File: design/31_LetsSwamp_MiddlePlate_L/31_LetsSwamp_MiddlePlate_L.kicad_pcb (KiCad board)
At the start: 2 copper layers, 122.6 x 85.3 mm, 0 parts

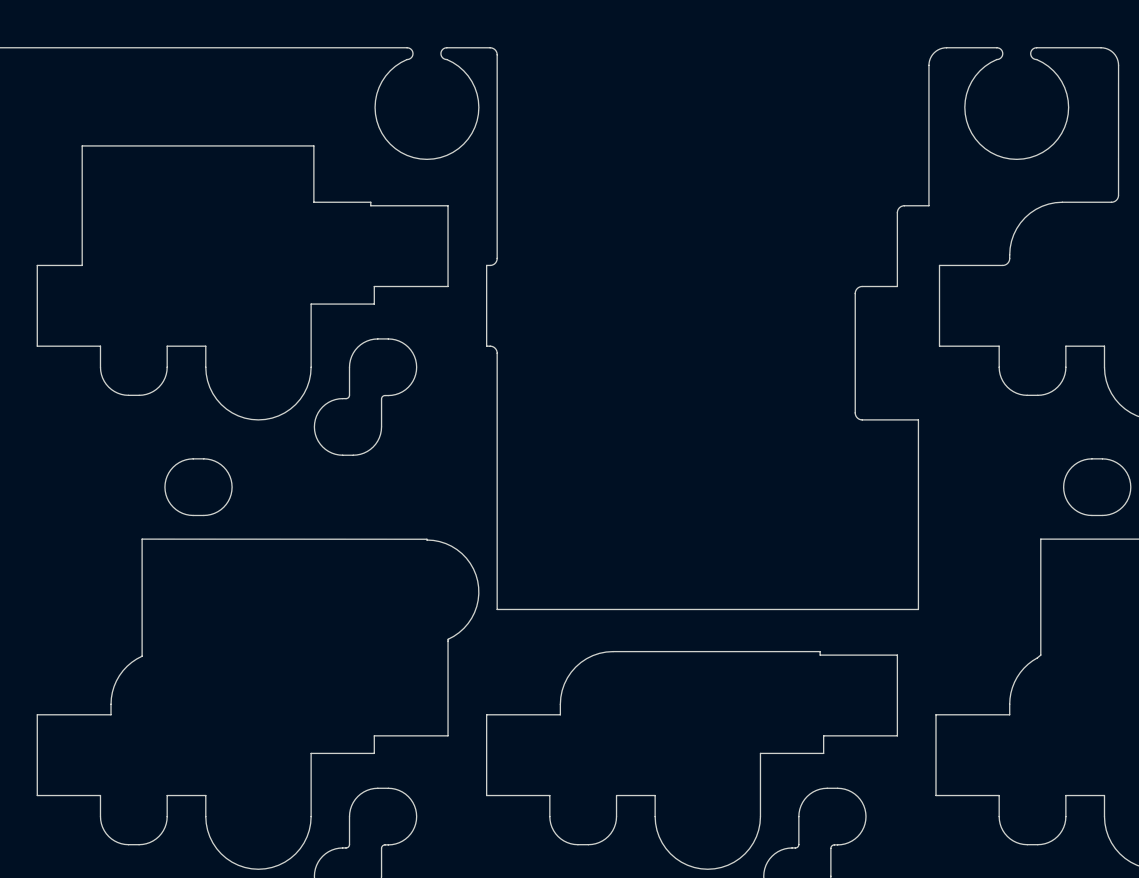
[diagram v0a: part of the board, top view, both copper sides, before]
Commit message: Modify middle plates
avoid to pin sockets and some diodes
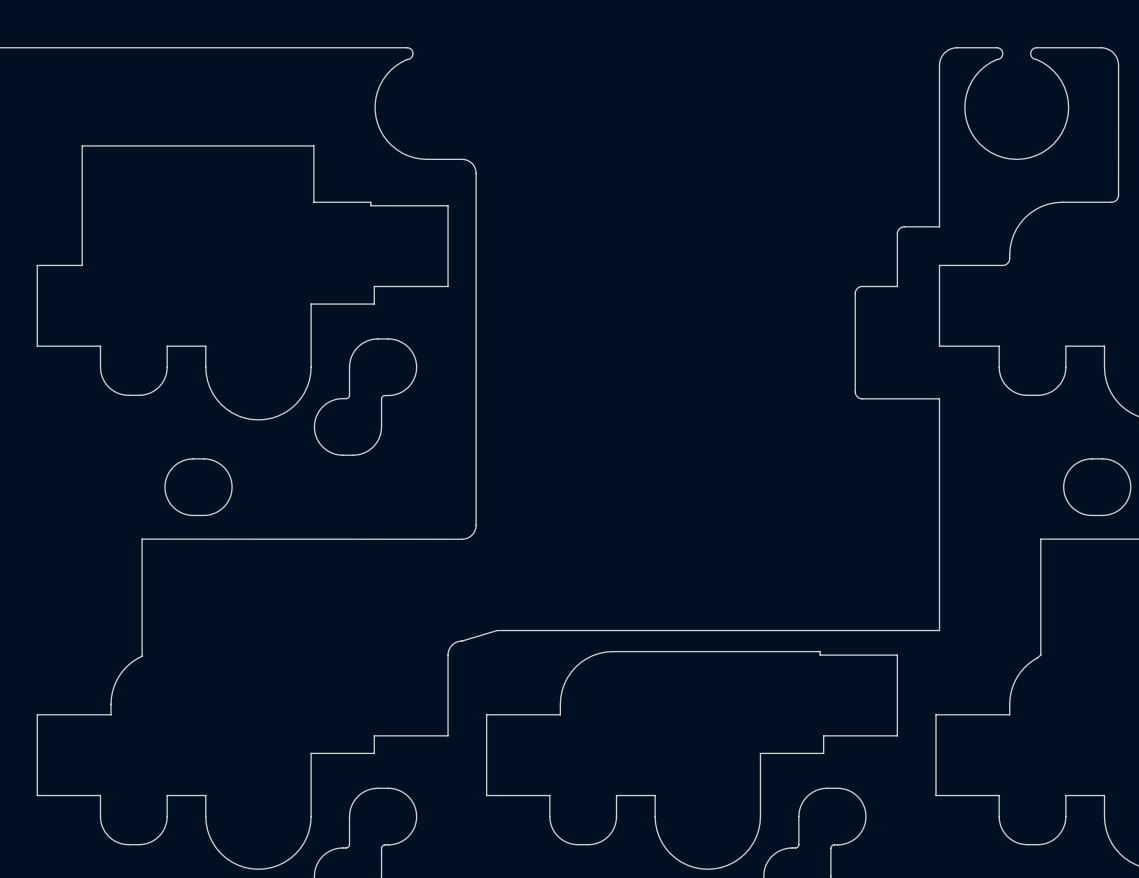
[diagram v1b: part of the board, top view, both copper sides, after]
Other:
- outline, holes or cut-outs redrawn
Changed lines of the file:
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@@
   (general
     (thickness 1.6)
-    (drawings 887)
+    (drawings 880)
     (tracks 0)
     (zones 0)
@@
     (38 B.Mask user)
     (39 F.Mask user)
-    (40 Dwgs.User user hide)
+    (40 Dwgs.User user)
     (41 Cmts.User user)
     (42 Eco1.User user)
@@
     (uvia_drill 0.1)
   )
+  (gr_line (start 65.782024 11.608585) (end 67.270256 11.162101) (layer Edge.Cuts) (width 0.05))
+  (gr_arc (start 65.782024 12.203897) (end 65.782024 11.608585) (angle -90) (layer Edge.Cuts) (width 0.05))
+  (gr_arc (start 65.781975 6.69726) (end 65.781975 7.292572) (angle -90) (layer Edge.Cuts) (width 0.05))
+  (gr_arc (start 65.781975 -8.217979) (end 66.377287 -8.217979) (angle -90) (layer Edge.Cuts) (width 0.05))
+  (gr_line (start 64.293688 -8.813291) (end 65.781975 -8.813291) (layer Edge.Cuts) (width 0.05))
   (gr_line (start -2.827732 69.605804) (end -2.827732 63.433855) (layer Edge.Cuts) (width 0.05))
   (gr_line (start 12.35274 59.305804) (end 12.35274 56.257032) (layer Edge.Cuts) (width 0.05))
@@
   (gr_arc (start 97.779996 -2.381248) (end 97.779996 -2.678904) (angle -90) (layer Edge.Cuts) (width 0.05))
   (gr_arc (start 100.4589 -3.125388) (end 100.4589 -3.423044) (angle -90) (layer Edge.Cuts) (width 0.05))
-  (gr_arc (start 82.748368 1.934764) (end 82.450712 1.934764) (angle -90) (layer Edge.Cuts) (width 0.05))
-  (gr_arc (start 66.9726 -0.595312) (end 67.270256 -0.595312) (angle -90) (layer Edge.Cuts) (width 0.05))
-  (gr_arc (start 66.9726 -4.613668) (end 66.9726 -4.316012) (angle -90) (layer Edge.Cuts) (width 0.05))
-  (gr_arc (start 66.9726 -13.245692) (end 67.270256 -13.245692) (angle -90) (layer Edge.Cuts) (width 0.05))
-  (gr_arc (start 84.534304 -6.548432) (end 84.534304 -6.846088) (angle -90) (layer Edge.Cuts) (width 0.05))
+  (gr_arc (start 82.748368 1.041795) (end 82.450712 1.041795) (angle -90) (layer Edge.Cuts) (width 0.05))
+  (gr_arc (start 84.534368 -5.655463) (end 84.534368 -5.953119) (angle -90) (layer Edge.Cuts) (width 0.05))
   (gr_arc (start 82.748368 -3.125388) (end 82.748368 -3.423044) (angle -90) (layer Edge.Cuts) (width 0.05))
   (gr_arc (start 88.701488 -4.613668) (end 88.701488 -4.316012) (angle -90) (layer Edge.Cuts) (width 0.05))
@@
     (arrow2b (pts (xy -15.64666 -13.551608) (xy -15.061963 -12.424208)))
   )
-  (gr_line (start 82.450712 1.934764) (end 82.450712 -3.125388) (layer Edge.Cuts) (width 0.05))
+  (gr_line (start 82.450712 1.041795) (end 82.450712 -3.125388) (layer Edge.Cuts) (width 0.05))
   (gr_circle (center 83.820064 3.740545) (end 85.091651 3.740545) (layer Dwgs.User) (width 0.05))
   (gr_circle (center 83.820064 6.280545) (end 85.091651 6.280545) (layer Dwgs.User) (width 0.05))
-  (gr_line (start 85.129616 10.269132) (end 67.270256 10.269132) (layer Edge.Cuts) (width 0.05))
+  (gr_line (start 86.022585 11.162101) (end 67.270256 11.162101) (layer Edge.Cuts) (width 0.05))
   (gr_circle (center 83.820064 8.820545) (end 85.091651 8.820545) (layer Dwgs.User) (width 0.05))
-  (gr_line (start 85.129616 2.232422) (end 85.129616 10.269132) (layer Edge.Cuts) (width 0.05))
-  (gr_line (start 82.748368 2.23242) (end 85.129616 2.232422) (layer Edge.Cuts) (width 0.05))
-  (gr_line (start 67.270256 10.269132) (end 67.270256 -0.595312) (layer Edge.Cuts) (width 0.05))
+  (gr_line (start 86.022585 1.339451) (end 86.022585 11.162101) (layer Edge.Cuts) (width 0.05))
+  (gr_line (start 82.748368 1.339451) (end 86.022585 1.339451) (layer Edge.Cuts) (width 0.05))
+  (gr_line (start 66.377287 6.69726) (end 66.377287 -8.217978) (layer Edge.Cuts) (width 0.05))
   (gr_line (start 65.186728 -6.846072) (end 61.912512 -6.846072) (layer Edge.Cuts) (width 0.05))
   (gr_line (start 61.912512 -6.846072) (end 61.912512 -6.9949) (layer Edge.Cuts) (width 0.05))
@@
   (gr_line (start 71.123217 31.371943) (end 71.26758 31.25388) (layer Edge.Cuts) (width 0.05))
   (gr_line (start 90.173198 12.321953) (end 90.317564 12.203896) (layer Edge.Cuts) (width 0.05))
-  (gr_line (start 64.293836 7.325009) (end 64.293696 7.292572) (layer Edge.Cuts) (width 0.05))
-  (gr_line (start 65.186712 11.608584) (end 65.191555 11.533514) (layer Edge.Cuts) (width 0.05))
-  (gr_arc (start 64.293836 9.525008) (end 64.293836 7.325009) (angle 155.9173345) (layer Edge.Cuts) (width 0.05))
   (gr_line (start 65.186664 49.708552) (end 65.182426 49.63757) (layer Edge.Cuts) (width 0.05))
   (gr_line (start 62.040228 47.767968) (end 62.093836 47.625008) (layer Edge.Cuts) (width 0.05))
@@
   (gr_arc (start 53.131644 33.337504) (end 50.899224 33.337504) (angle 65.83806624) (layer Edge.Cuts) (width 0.05))
   (gr_line (start 52.21758 7.286704) (end 52.21758 12.25) (layer Edge.Cuts) (width 0.05))
-  (gr_line (start 65.186712 15.626956) (end 65.186712 11.608584) (layer Edge.Cuts) (width 0.05))
+  (gr_line (start 65.186712 15.626956) (end 65.186712 12.203897) (layer Edge.Cuts) (width 0.05))
   (gr_line (start 50.899224 14.733988) (end 47.773836 14.733988) (layer Edge.Cuts) (width 0.05))
   (gr_line (start 59.38242 19.05) (end 59.38242 16.371096) (layer Edge.Cuts) (width 0.05))
   (gr_line (start 62.061324 15.626956) (end 65.186712 15.626956) (layer Edge.Cuts) (width 0.05))
   (gr_line (start 50.899224 14.287504) (end 50.899224 14.733988) (layer Edge.Cuts) (width 0.05))
-  (gr_line (start 64.293696 7.292572) (end 52.21758 7.286704) (layer Edge.Cuts) (width 0.05))
+  (gr_line (start 65.781975 7.292572) (end 52.21758 7.286704) (layer Edge.Cuts) (width 0.05))
   (gr_line (start 54.91758 19.05) (end 54.91758 18.157032) (layer Edge.Cuts) (width 0.05))
   (gr_arc (start 57.15 19.05) (end 54.91758 19.05) (angle -180) (layer Edge.Cuts) (width 0.05))
@@
   (gr_line (start 4.890228 -6.846088) (end 4.890228 -9.382032) (layer Edge.Cuts) (width 0.05))
   (gr_line (start -4.93242 -9.382032) (end -4.93242 -6.8) (layer Edge.Cuts) (width 0.05))
-  (gr_arc (start 86.321412 -12.799208) (end 85.5761 -12.799208) (angle 90) (layer Edge.Cuts) (width 0.05))
-  (gr_line (start 67.270256 -4.613668) (end 67.270256 -13.245692) (layer Edge.Cuts) (width 0.05))
-  (gr_line (start 65.13574 -13.54452) (end 66.9726 -13.543348) (layer Edge.Cuts) (width 0.05))
+  (gr_arc (start 86.767897 -12.799208) (end 86.022585 -12.799208) (angle 90) (layer Edge.Cuts) (width 0.05))
   (gr_arc (start 63.451931 -13.295173) (end 63.451931 -13.045826) (angle -179.9997702) (layer Edge.Cuts) (width 0.05))
-  (gr_arc (start 65.13574 -13.295173) (end 65.13574 -13.54452) (angle -179.9997702) (layer Edge.Cuts) (width 0.05))
-  (gr_arc (start 64.293836 -11.013291) (end 63.451932 -13.045826) (angle -315) (layer Edge.Cuts) (width 0.05))
-  (gr_line (start 85.5761 -6.846088) (end 84.534304 -6.846088) (layer Edge.Cuts) (width 0.05))
-  (gr_line (start 84.236712 -3.423044) (end 84.236648 -6.548432) (layer Edge.Cuts) (width 0.05))
+  (gr_arc (start 64.293836 -11.013291) (end 63.451932 -13.045826) (angle -157.4961397) (layer Edge.Cuts) (width 0.05))
+  (gr_line (start 86.022585 -5.953119) (end 84.534368 -5.953119) (layer Edge.Cuts) (width 0.05))
+  (gr_line (start 84.236712 -3.423044) (end 84.236712 -5.655463) (layer Edge.Cuts) (width 0.05))
   (gr_line (start 82.748368 -3.423044) (end 84.236712 -3.423044) (layer Edge.Cuts) (width 0.05))
-  (gr_line (start 66.823836 -0.892968) (end 66.9726 -0.892968) (layer Edge.Cuts) (width 0.05))
-  (gr_line (start 66.823836 -4.316012) (end 66.823836 -0.892968) (layer Edge.Cuts) (width 0.05))
-  (gr_line (start 66.9726 -4.316012) (end 66.823836 -4.316012) (layer Edge.Cuts) (width 0.05))
   (gr_line (start 100.161324 15.626956) (end 103.286712 15.626956) (layer Edge.Cuts) (width 0.05))
   (gr_line (start 88.999224 14.733988) (end 85.873836 14.733988) (layer Edge.Cuts) (width 0.05))
@@
   (gr_line (start 93.612812 -7.292572) (end 93.613984 -12.799208) (layer Edge.Cuts) (width 0.05))
   (gr_line (start 108.183696 -6.698432) (end 103.584288 -6.69726) (layer Edge.Cuts) (width 0.05))
-  (gr_line (start 86.32024 -13.54452) (end 88.455046 -13.54452) (layer Edge.Cuts) (width 0.05))
-  (gr_line (start 85.5761 -6.846088) (end 85.5761 -12.799208) (layer Edge.Cuts) (width 0.05))
+  (gr_line (start 86.767897 -13.54452) (end 88.455046 -13.54452) (layer Edge.Cuts) (width 0.05))
+  (gr_line (start 86.022585 -5.953119) (end 86.022585 -12.799208) (layer Edge.Cuts) (width 0.05))
   (gr_line (start -13.675008 8.683104) (end -13.675008 -9.413291) (layer Edge.Cuts) (width 0.05))
   (gr_line (start -8.876164 -13.54452) (end 63.451932 -13.54452) (layer Edge.Cuts) (width 0.05))
